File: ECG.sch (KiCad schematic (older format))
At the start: 19 parts, among them J1 SJ-3566AN, U1 ADR4525, U2 SP6641

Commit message: #7 - Add ADC
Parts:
- removed Pgnd1, Pgnd2, Vo1: MountingHole_Pad, MountingHole:MountingHole_6mm_Pad_Via, symbol Mechanical:MountingHole_Pad
- added C15: 0.1u, Capacitor_SMD:C_0805_2012Metric_Pad1.18x1.45mm_HandSolder, symbol Device:C
- added J2: Conn_01x02_Male, Connector_PinHeader_2.00mm:PinHeader_1x02_P2.00mm_Vertical, symbol Connector:Conn_01x02_Male
- added R22, R23: 10k, Resistor_SMD:R_0805_2012Metric_Pad1.20x1.40mm_HandSolder, symbol Device:R
- added R24, R25: 3.3k, Resistor_SMD:R_0805_2012Metric_Pad1.20x1.40mm_HandSolder, symbol Device:R
- added U7: ADS1015IDGS, Package_SO:TSSOP-10_3x3mm_P0.5mm, symbol Analog_ADC:ADS1015IDGS
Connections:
- wire segments 43 -> 58
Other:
- note added: "Should I have some sort of resistance on the 2.5V input?\n"
- note added: "Tie to supply to reduce leakage currents."
- moved on the sheet: C14, J1, R20, S1

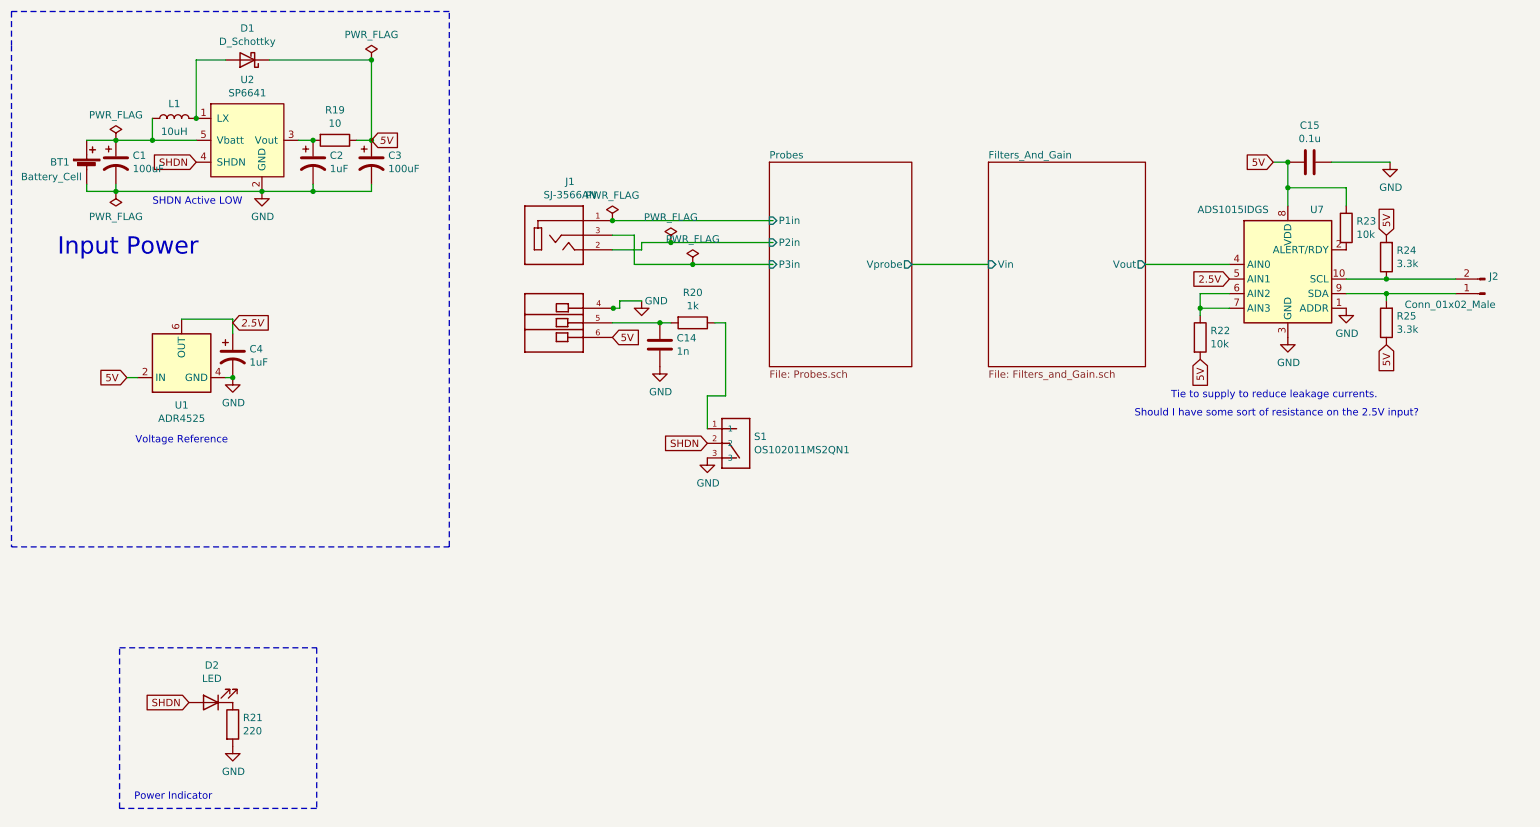
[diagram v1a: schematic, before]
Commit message: #9 - Add heartbeat indicator
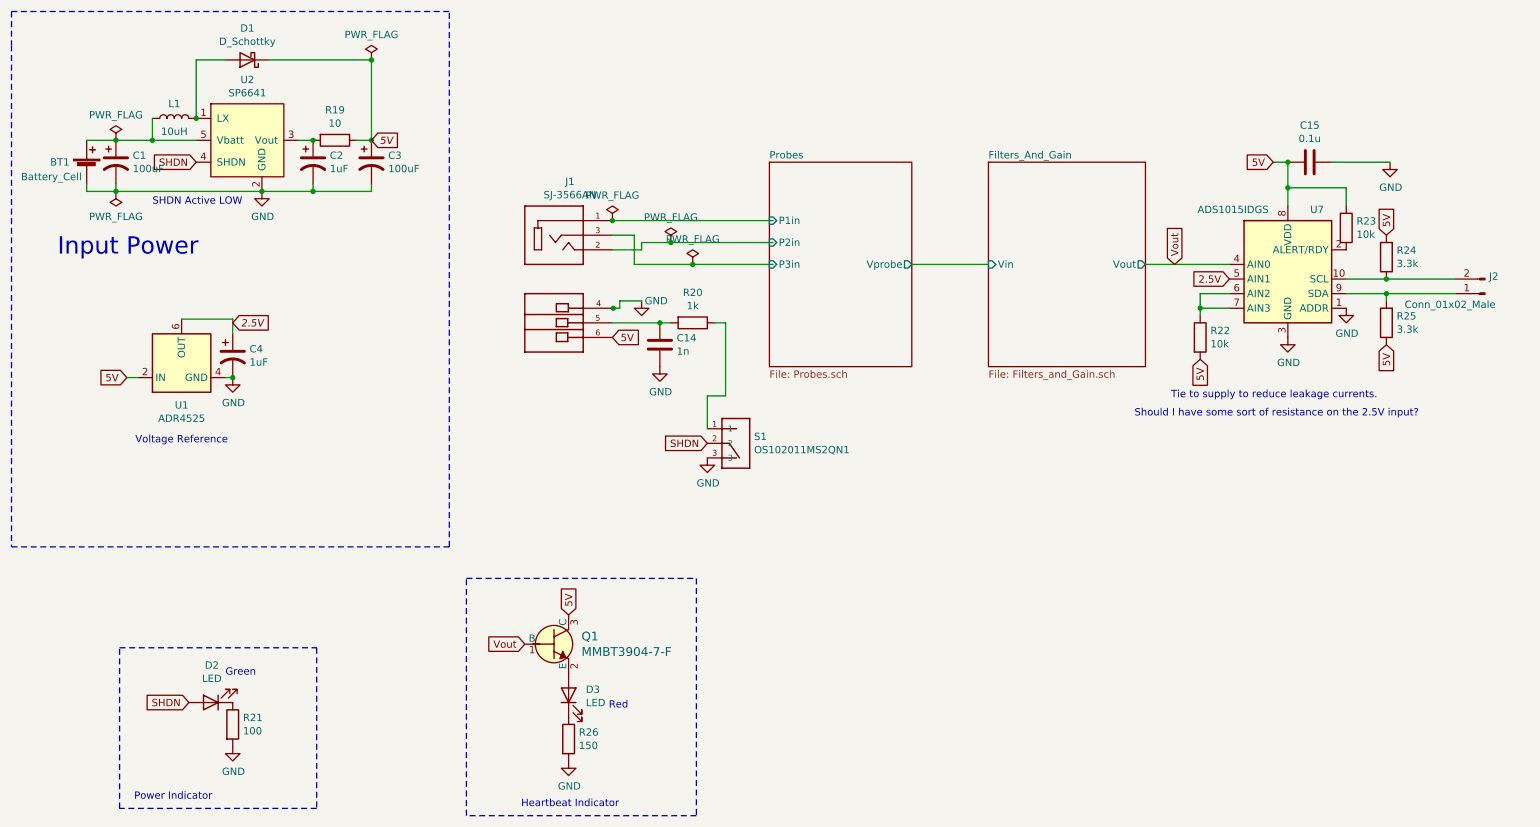
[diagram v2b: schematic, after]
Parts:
- added D3: LED, Diode_SMD:D_0603_1608Metric_Pad1.05x0.95mm_HandSolder, symbol Device:LED
- added Q1: MMBT3904-7-F, digikey-footprints:SOT-23-3, symbol dk_Transistors-Bipolar-BJT-Single:MMBT3904-7-F
- added R26: 150, Resistor_SMD:R_0805_2012Metric_Pad1.20x1.40mm_HandSolder, symbol Device:R
- R21: value 220 -> 100
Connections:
- net labels added: Vout
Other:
- note added: "Green\n"
- note added: "Heartbeat Indicator\n"
- note added: "Red"
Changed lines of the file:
@@
 P 2400 6650
 F 0 "R21" H 2470 6696 50  0000 L CNN
-F 1 "220" H 2470 6605 50  0000 L CNN
+F 1 "100" H 2470 6605 50  0000 L CNN
 F 2 "Resistor_SMD:R_0805_2012Metric_Pad1.20x1.40mm_HandSolder" V 2330 6650 50  0001 C CNN
 F 3 "~" H 2400 6650 50  0001 C CNN
@@
 F 1 "LED" H 2243 6336 50  0000 C CNN
 F 2 "Diode_SMD:D_0603_1608Metric_Pad1.05x0.95mm_HandSolder" H 2250 6500 50  0001 C CNN
-F 3 "~" H 2250 6500 50  0001 C CNN
+F 3 "http://www.qt-brightek.com/datasheet/QBLP601_series.pdf" H 2250 6500 50  0001 C CNN
 	1    2250 6500
 	-1   0    0    1
@@
 Wire Wire Line
 	7050 3500 7575 3500
+Text Notes 2350 6325 0    50   ~ 0
+Green\n
+$Comp
+L dk_Transistors-Bipolar-BJT-Single:MMBT3904-7-F Q1
+U 1 1 5FC76954
+P 4600 6100
+F 0 "Q1" H 4788 6153 60  0000 L CNN
+F 1 "MMBT3904-7-F" H 4788 6047 60  0000 L CNN
+F 2 "digikey-footprints:SOT-23-3" H 4800 6300 60  0001 L CNN
+F 3 "https://www.diodes.com/assets/Datasheets/ds30036.pdf" H 4800 6400 60  0001 L CNN
+F 4 "MMBT3904-FDICT-ND" H 4800 6500 60  0001 L CNN "Digi-Key_PN"
+F 5 "MMBT3904-7-F" H 4800 6600 60  0001 L CNN "MPN"
+F 6 "Discrete Semiconductor Products" H 4800 6700 60  0001 L CNN "Category"
+F 7 "Transistors - Bipolar (BJT) - Single" H 4800 6800 60  0001 L CNN "Family"
+F 8 "https://www.diodes.com/assets/Datasheets/ds30036.pdf" H 4800 6900 60  0001 L CNN "DK_Datasheet_Link"
+F 9 "/product-detail/en/diodes-incorporated/MMBT3904-7-F/MMBT3904-FDICT-ND/815727" H 4800 7000 60  0001 L CNN "DK_Detail_Page"
+F 10 "TRANS NPN 40V 0.2A SMD SOT23-3" H 4800 7100 60  0001 L CNN "Description"
+F 11 "Diodes Incorporated" H 4800 7200 60  0001 L CNN "Manufacturer"
+F 12 "Active" H 4800 7300 60  0001 L CNN "Status"
+	1    4600 6100
+	1    0    0    -1
+$EndComp
+Text GLabel 8850 3500 1    50   Input ~ 0
+Vout
+Text GLabel 4400 6100 0    50   Input ~ 0
+Vout
+Text GLabel 4700 5900 1    50   Input ~ 0
+5V
+$Comp
+L Device:R R26
+U 1 1 5FC7A644
+P 4700 6750
+F 0 "R26" H 4770 6796 50  0000 L CNN
+F 1 "150" H 4770 6705 50  0000 L CNN
+F 2 "Resistor_SMD:R_0805_2012Metric_Pad1.20x1.40mm_HandSolder" V 4630 6750 50  0001 C CNN
+F 3 "~" H 4700 6750 50  0001 C CNN
+	1    4700 6750
+	1    0    0    -1
+$EndComp
+$Comp
+L Device:LED D3
+U 1 1 5FC7B21A
+P 4700 6450
+F 0 "D3" V 4739 6332 50  0000 R CNN
+F 1 "LED" V 4648 6332 50  0000 R CNN
+F 2 "Diode_SMD:D_0603_1608Metric_Pad1.05x0.95mm_HandSolder" H 4700 6450 50  0001 C CNN
+F 3 "https://www.we-online.de/katalog/datasheet/150060RS75000.pdf" H 4700 6450 50  0001 C CNN
+	1    4700 6450
+	0    -1   -1   0
+$EndComp
+Text Notes 4975 6550 0    50   ~ 0
+Red
+$Comp
+L power:GND #PWR03
+U 1 1 5FC7D95F
+P 4700 6900
+F 0 "#PWR03" H 4700 6650 50  0001 C CNN
+F 1 "GND" H 4705 6727 50  0000 C CNN
+F 2 "" H 4700 6900 50  0001 C CNN
+F 3 "" H 4700 6900 50  0001 C CNN
+	1    4700 6900
+	1    0    0    -1
+$EndComp
+Wire Notes Line
+	4000 5650 5575 5650
+Wire Notes Line
+	5575 5650 5575 7275
+Wire Notes Line
+	5575 7275 4000 7275
+Wire Notes Line
+	4000 7275 4000 5650
+Text Notes 4375 7225 0    50   ~ 0
+Heartbeat Indicator\n
 $EndSCHEMATC

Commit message: #8 - Add test points. (Also updated filter circuit)
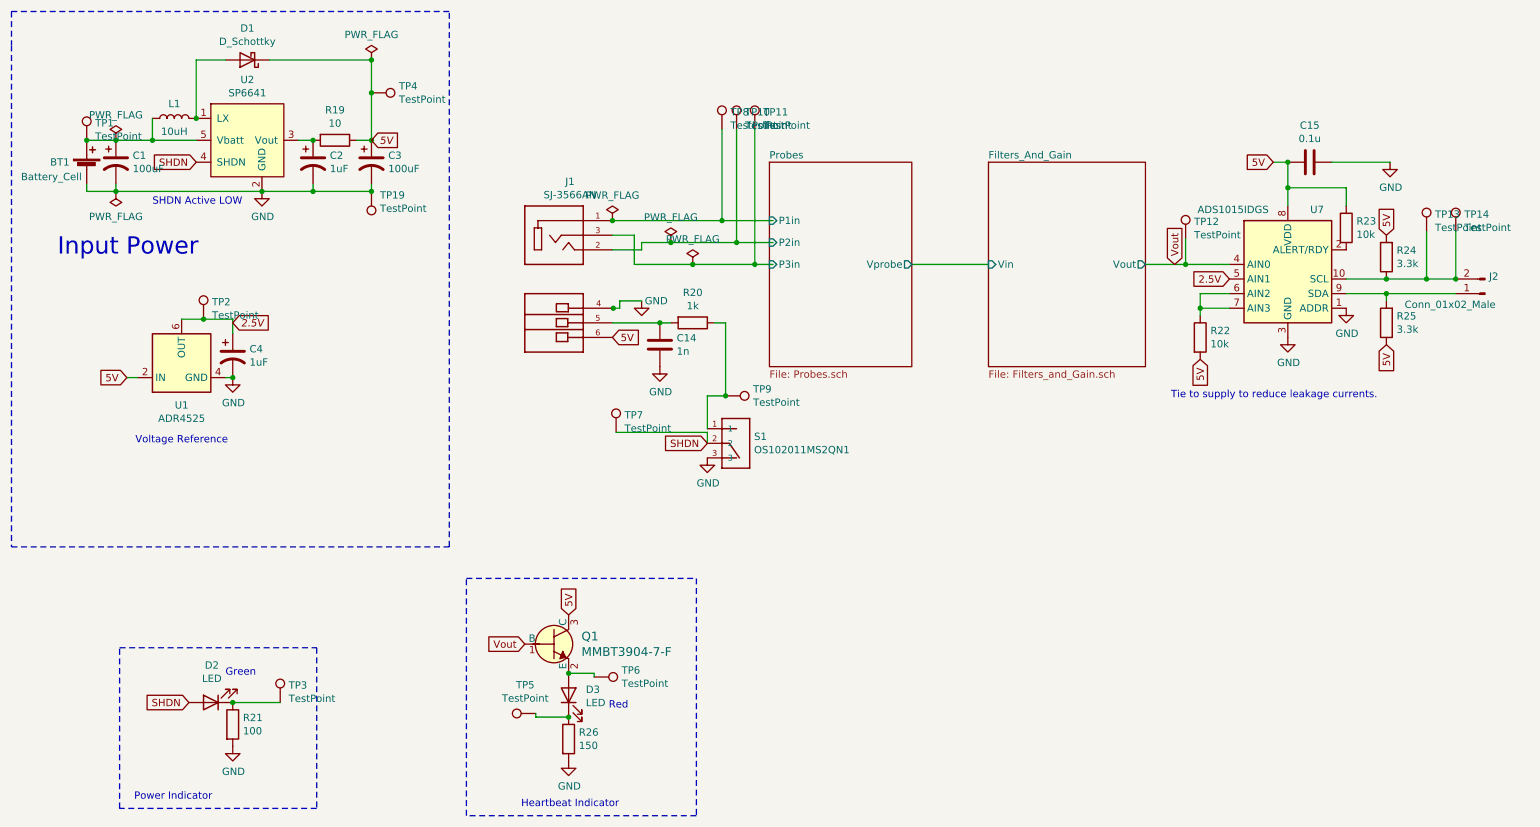
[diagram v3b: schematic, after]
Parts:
- added TP1, TP10, TP11, TP12, TP13, TP14, TP3, TP5, TP6, TP7, TP8, TP9: TestPoint, TestPoint:TestPoint_Pad_D2.0mm, symbol Connector:TestPoint
- added TP19, TP2, TP4: TestPoint, TestPoint:TestPoint_Pad_D4.0mm, symbol Connector:TestPoint
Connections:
- wire segments 58 -> 78
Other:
- note removed: "Should I have some sort of resistance on the 2.5V input?\n"
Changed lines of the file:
@@
 $EndComp
 Wire Wire Line
-	2050 3875 2400 3875
+	2050 3875 2200 3875
 Wire Wire Line
 	2400 3875 2400 3975
@@
 	2650 2100 3350 2100
 Wire Wire Line
-	3350 2100 3350 2650
+	3350 2100 3350 2325
 Wire Wire Line
 	3350 2650 3250 2650
@@
 Wire Wire Line
 	5150 3500 5550 3500
-Wire Wire Line
-	6100 3200 5000 3200
 $Comp
 L power:PWR_FLAG #FLG0104
@@
 $EndComp
 Connection ~ 5400 3350
-Wire Wire Line
-	5400 3350 6100 3350
 $Comp
 L power:PWR_FLAG #FLG02
@@
 $EndComp
 Connection ~ 5550 3500
-Wire Wire Line
-	5550 3500 6100 3500
 $Comp
 L Switches:OS102011MS2QN1 S1
@@
 Connection ~ 10300 3700
 Wire Wire Line
-	10300 3600 10775 3600
+	10300 3600 10575 3600
 Wire Wire Line
 	10300 3600 10025 3600
@@
 $EndComp
 Wire Wire Line
-	8650 3500 9225 3500
+	8650 3500 8925 3500
 Text GLabel 9225 3600 0    50   Input ~ 0
 2.5V
@@
 Text Notes 8825 4425 0    50   ~ 0
 Tie to supply to reduce leakage currents.
-Text Notes 8575 4550 0    50   ~ 0
-Should I have some sort of resistance on the 2.5V input?\n
 Wire Wire Line
 	9925 2800 10325 2800
@@
 Text Notes 4375 7225 0    50   ~ 0
 Heartbeat Indicator\n
+Wire Wire Line
+	5000 3200 5750 3200
+Wire Wire Line
+	5400 3350 5850 3350
+Wire Wire Line
+	5550 3500 5975 3500
+$Comp
+L Connector:TestPoint TP11
+U 1 1 5FC76706
+P 5975 2575
+F 0 "TP11" H 6033 2693 50  0000 L CNN
+F 1 "TestPoint" H 6033 2602 50  0000 L CNN
+F 2 "TestPoint:TestPoint_Pad_D2.0mm" H 6175 2575 50  0001 C CNN
+F 3 "~" H 6175 2575 50  0001 C CNN
+	1    5975 2575
+	1    0    0    -1
+$EndComp
+$Comp
+L Connector:TestPoint TP10
+U 1 1 5FC772A9
+P 5850 2575
+F 0 "TP10" H 5908 2693 50  0000 L CNN
+F 1 "TestPoint" H 5908 2602 50  0000 L CNN
+F 2 "TestPoint:TestPoint_Pad_D2.0mm" H 6050 2575 50  0001 C CNN
+F 3 "~" H 6050 2575 50  0001 C CNN
+	1    5850 2575
+	1    0    0    -1
+$EndComp
+$Comp
+L Connector:TestPoint TP8
+U 1 1 5FC7781D
+P 5750 2575
+F 0 "TP8" H 5808 2693 50  0000 L CNN
+F 1 "TestPoint" H 5808 2602 50  0000 L CNN
+F 2 "TestPoint:TestPoint_Pad_D2.0mm" H 5950 2575 50  0001 C CNN
+F 3 "~" H 5950 2575 50  0001 C CNN
+	1    5750 2575
+	1    0    0    -1
+$EndComp
+Wire Wire Line
+	5750 2575 5750 3200
+Connection ~ 5750 3200
+Wire Wire Line
+	5750 3200 6100 3200
+Wire Wire Line
+	5850 2575 5850 3350
+Connection ~ 5850 3350
+Wire Wire Line
+	5850 3350 6100 3350
+Wire Wire Line
+	5975 2575 5975 3500
+Connection ~ 5975 3500
+Wire Wire Line
+	5975 3500 6100 3500
+$Comp
+L Connector:TestPoint TP9
+U 1 1 5FC7C756
+P 5775 4400
+F 0 "TP9" V 5729 4588 50  0000 L CNN
+F 1 "TestPoint" V 5820 4588 50  0000 L CNN
+F 2 "TestPoint:TestPoint_Pad_D2.0mm" H 5975 4400 50  0001 C CNN
+F 3 "~" H 5975 4400 50  0001 C CNN
+	1    5775 4400
+	0    1    1    0
+$EndComp
+Connection ~ 5775 4400
+$Comp
+L Connector:TestPoint TP6
+U 1 1 5FC7D0FE
+P 4875 6325
+F 0 "TP6" V 4829 6513 50  0000 L CNN
+F 1 "TestPoint" V 4920 6513 50  0000 L CNN
+F 2 "TestPoint:TestPoint_Pad_D2.0mm" H 5075 6325 50  0001 C CNN
+F 3 "~" H 5075 6325 50  0001 C CNN
+	1    4875 6325
+	0    1    1    0
+$EndComp
+$Comp
+L Connector:TestPoint TP5
+U 1 1 5FC7E935
+P 4475 6575
+F 0 "TP5" V 4670 6647 50  0000 C CNN
+F 1 "TestPoint" V 4579 6647 50  0000 C CNN
+F 2 "TestPoint:TestPoint_Pad_D2.0mm" H 4675 6575 50  0001 C CNN
+F 3 "~" H 4675 6575 50  0001 C CNN
+	1    4475 6575
+	0    -1   -1   0
+$EndComp
+Wire Wire Line
+	4700 6600 4475 6600
+Wire Wire Line
+	4475 6600 4475 6575
+Connection ~ 4700 6600
+$Comp
+L Connector:TestPoint TP3
+U 1 1 5FC8361A
+P 2725 6500
+F 0 "TP3" H 2783 6618 50  0000 L CNN
+F 1 "TestPoint" H 2783 6527 50  0000 L CNN
+F 2 "TestPoint:TestPoint_Pad_D2.0mm" H 2925 6500 50  0001 C CNN
+F 3 "~" H 2925 6500 50  0001 C CNN
+	1    2725 6500
+	1    0    0    -1
+$EndComp
+Wire Wire Line
+	2725 6500 2400 6500
+Connection ~ 2400 6500
+$Comp
+L Connector:TestPoint TP2
+U 1 1 5FC87C23
+P 2200 3875
+F 0 "TP2" H 2258 3993 50  0000 L CNN
+F 1 "TestPoint" H 2258 3902 50  0000 L CNN
+F 2 "TestPoint:TestPoint_Pad_D4.0mm" H 2400 3875 50  0001 C CNN
+F 3 "~" H 2400 3875 50  0001 C CNN
+	1    2200 3875
+	1    0    0    -1
+$EndComp
+Connection ~ 2200 3875
+Wire Wire Line
+	2200 3875 2400 3875
+$Comp
+L Connector:TestPoint TP4
+U 1 1 5FC8907B
+P 3350 2325
+F 0 "TP4" V 3304 2513 50  0000 L CNN
+F 1 "TestPoint" V 3395 2513 50  0000 L CNN
+F 2 "TestPoint:TestPoint_Pad_D4.0mm" H 3550 2325 50  0001 C CNN
+F 3 "~" H 3550 2325 50  0001 C CNN
+	1    3350 2325
+	0    1    1    0
+$EndComp
+Connection ~ 3350 2325
+Wire Wire Line
+	3350 2325 3350 2650
+$Comp
+L Connector:TestPoint TP1
+U 1 1 5FC8A574
+P 1400 2650
+F 0 "TP1" H 1458 2768 50  0000 L CNN
+F 1 "TestPoint" H 1458 2677 50  0000 L CNN
+F 2 "TestPoint:TestPoint_Pad_D2.0mm" H 1600 2650 50  0001 C CNN
+F 3 "~" H 1600 2650 50  0001 C CNN
+	1    1400 2650
+	1    0    0    -1
+$EndComp
+Connection ~ 1400 2650
+$Comp
+L Connector:TestPoint TP7
+U 1 1 5FC8DB2C
+P 5025 4650
+F 0 "TP7" H 5083 4768 50  0000 L CNN
+F 1 "TestPoint" H 5083 4677 50  0000 L CNN
+F 2 "TestPoint:TestPoint_Pad_D2.0mm" H 5225 4650 50  0001 C CNN
+F 3 "~" H 5225 4650 50  0001 C CNN
+	1    5025 4650
+	1    0    0    -1
+$EndComp
+Wire Wire Line
+	5025 4650 5650 4650
+Wire Wire Line
+	5650 4725 5650 4650
+$Comp
+L Connector:TestPoint TP14
+U 1 1 5FC95E35
+P 10775 3275
+F 0 "TP14" H 10833 3393 50  0000 L CNN
+F 1 "TestPoint" H 10833 3302 50  0000 L CNN
+F 2 "TestPoint:TestPoint_Pad_D2.0mm" H 10975 3275 50  0001 C CNN
+F 3 "~" H 10975 3275 50  0001 C CNN
+	1    10775 3275
+	1    0    0    -1
+$EndComp
+$Comp
+L Connector:TestPoint TP13
+U 1 1 5FC9653A
+P 10575 3275
+F 0 "TP13" H 10633 3393 50  0000 L CNN
+F 1 "TestPoint" H 10633 3302 50  0000 L CNN
+F 2 "TestPoint:TestPoint_Pad_D2.0mm" H 10775 3275 50  0001 C CNN
+F 3 "~" H 10775 3275 50  0001 C CNN
+	1    10575 3275
+	1    0    0    -1
+$EndComp
+Wire Wire Line
+	10575 3275 10575 3600
+Connection ~ 10575 3600
+Wire Wire Line
+	10575 3600 10775 3600
+Connection ~ 10775 3600
+Wire Wire Line
+	10775 3275 10775 3600
+$Comp
+L Connector:TestPoint TP12
+U 1 1 5FCA6AF9
+P 8925 3325
+F 0 "TP12" H 8983 3443 50  0000 L CNN
+F 1 "TestPoint" H 8983 3352 50  0000 L CNN
+F 2 "TestPoint:TestPoint_Pad_D2.0mm" H 9125 3325 50  0001 C CNN
+F 3 "~" H 9125 3325 50  0001 C CNN
+	1    8925 3325
+	1    0    0    -1
+$EndComp
+Wire Wire Line
+	8925 3325 8925 3500
+Connection ~ 8925 3500
+Wire Wire Line
+	8925 3500 9225 3500
+Wire Wire Line
+	4700 6300 4875 6300
+Wire Wire Line
+	4875 6300 4875 6325
+Connection ~ 4700 6300
+$Comp
+L Connector:TestPoint TP19
+U 1 1 5FCD9479
+P 3350 3000
+F 0 "TP19" H 3292 3026 50  0000 R CNN
+F 1 "TestPoint" H 3292 3117 50  0000 R CNN
+F 2 "TestPoint:TestPoint_Pad_D4.0mm" H 3550 3000 50  0001 C CNN
+F 3 "~" H 3550 3000 50  0001 C CNN
+	1    3350 3000
+	-1   0    0    1
+$EndComp
+Connection ~ 3350 3000
 $EndSCHEMATC

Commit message: #4 - Added the heart edge cut and updated the Kicad footprints that were removed
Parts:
- C2, C4: footprint Capacitor_SMD:C_0805_2012Metric_Pad1.15x1.40mm_HandSolder -> Capacitor_SMD:C_0805_2012Metric_Pad1.18x1.45mm_HandSolder
- R19: footprint Resistor_SMD:R_0805_2012Metric_Pad1.15x1.40mm_HandSolder -> Resistor_SMD:R_0805_2012Metric_Pad1.20x1.40mm_HandSolder
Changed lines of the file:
@@
 F 0 "C4" H 2515 4171 50  0000 L CNN
 F 1 "1uF" H 2515 4080 50  0000 L CNN
-F 2 "Capacitor_SMD:C_0805_2012Metric_Pad1.15x1.40mm_HandSolder" H 2400 4125 50  0001 C CNN
+F 2 "Capacitor_SMD:C_0805_2012Metric_Pad1.18x1.45mm_HandSolder" H 2400 4125 50  0001 C CNN
 F 3 "~" H 2400 4125 50  0001 C CNN
 	1    2400 4125
@@
 F 0 "C2" H 3065 2846 50  0000 L CNN
 F 1 "1uF" H 3065 2755 50  0000 L CNN
-F 2 "Capacitor_SMD:C_0805_2012Metric_Pad1.15x1.40mm_HandSolder" H 2950 2800 50  0001 C CNN
+F 2 "Capacitor_SMD:C_0805_2012Metric_Pad1.18x1.45mm_HandSolder" H 2950 2800 50  0001 C CNN
 F 3 "~" H 2950 2800 50  0001 C CNN
 	1    2950 2800
@@
 F 0 "R19" V 2893 2650 50  0000 C CNN
 F 1 "10" V 2984 2650 50  0000 C CNN
-F 2 "Resistor_SMD:R_0805_2012Metric_Pad1.15x1.40mm_HandSolder" V 3030 2650 50  0001 C CNN
+F 2 "Resistor_SMD:R_0805_2012Metric_Pad1.20x1.40mm_HandSolder" V 3030 2650 50  0001 C CNN
 F 3 "~" H 3100 2650 50  0001 C CNN
 	1    3100 2650
